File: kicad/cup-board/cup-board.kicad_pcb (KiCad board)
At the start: 4 copper layers, 68 x 68 mm, 102 parts, among them J2 EARCUP_SPKR, J7 CUP_IN (A2B + panel audio, ma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, J8 CUP_OUT (A2B to next cup), Q1 AO3401A, Q2 MMBT3904, U1 ADAU1861, U2 LSM6DSV16BX, U3 MAXM86161, U4 AQW612S, U5 AQW612S, U6 AD2428WBCPZ (sub-node), U7 TPS62161DSG (1V8), U8 ADP7118AUJZ-3.3-R7 (3V3_MIC), U9 ADP7118AUJZ-3.3-R7 (VLED)

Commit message: [LIMA] cup PCB: In1 GND / In2 1V8 planes + plane fanout; generic routing scripts in kicad/lib/route
kicad/lib/route: board-agnostic copies of the audio-board route tools (outline-based edge checks
for ring boards, env-driven plane/aircraft/fine nets, relative DSN tweaks, planes.py).
Cup: 94 pad vias + 20 EP vias, DRC 0, 153 unconnected (to route). All parts on top (Peter).

Co-Authored-By: Claude Opus 5.5 <noreply@anthropic.com>
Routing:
- net /GND: track 0.00 -> 29.2 mm, vias 0 -> 87
- net /1V8: track 0.00 -> 11.6 mm, vias 0 -> 27
- added copper zone on In2.Cu, net /1V8
- added copper zone on In1.Cu, net /GND

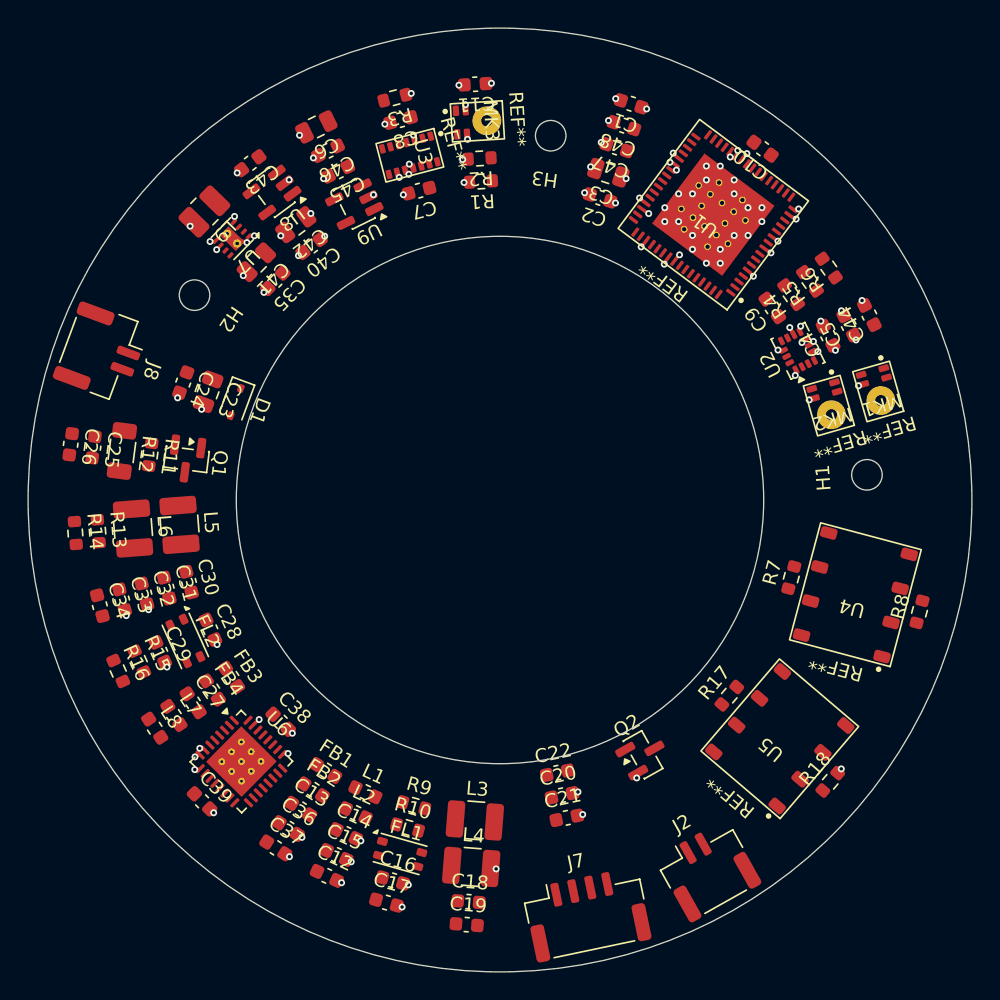
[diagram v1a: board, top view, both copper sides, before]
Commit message: [LIMA] cup PCB: Freerouting pass (WIP) - 9 unconnected; hole-clearance/neckdown fixes pending
DSN: In2 forced to plane (PLANE_LAYERS), outline inset 0.4 mm for the 0.5 mm edge rule (EDGE_INSET).

Co-Authored-By: Claude Opus 5.5 <noreply@anthropic.com>
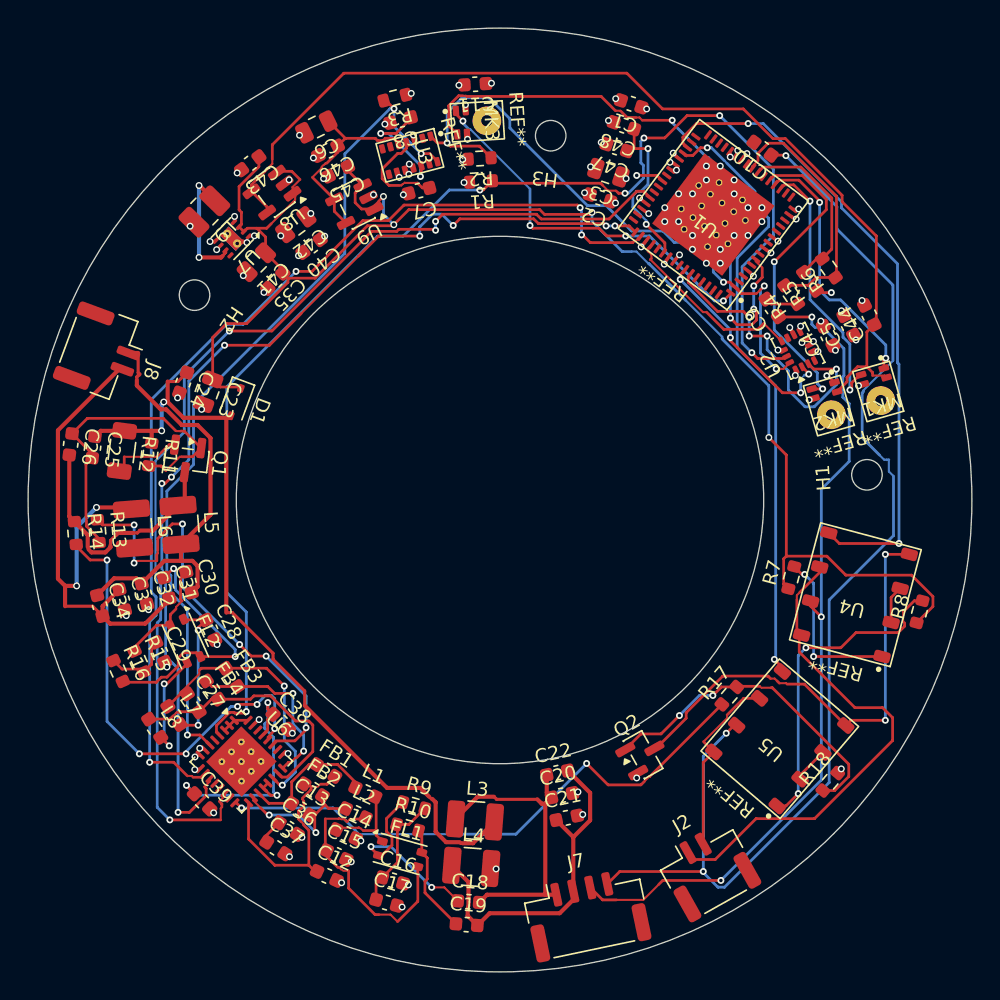
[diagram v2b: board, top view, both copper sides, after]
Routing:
- net /VIN_CUP: track 0.00 -> 112.3 mm, vias 0 -> 4
- net /SCL: track 0.00 -> 96.2 mm, vias 0 -> 6
- net /XF_SEC_B: track 0.00 -> 85.0 mm, vias 0 -> 3
- net /I2S0_SDATAO: track 0.00 -> 79.3 mm, vias 0 -> 4
- net /I2S0_FSYNC: track 0.00 -> 75.0 mm, vias 0 -> 8
- net /I2S0_BCLK: track 0.00 -> 74.5 mm, vias 0 -> 4
- net /3V3_MIC: track 0.00 -> 71.4 mm
- net /PPG_INT: track 0.00 -> 61.1 mm, vias 0 -> 3
- net /XF_SEC_A: track 0.00 -> 60.2 mm, vias 0 -> 3
- net /V_NODE: track 0.00 -> 59.5 mm, vias 0 -> 2
- net /HPOUTN: track 0.00 -> 46.8 mm, vias 0 -> 2
- net /SDA: track 0.00 -> 45.3 mm, vias 0 -> 4
- net /HPOUTP: track 0.00 -> 44.4 mm, vias 0 -> 2
- net /DMIC_CLK: track 0.00 -> 43.7 mm, vias 0 -> 4
- net /K2_CTL: track 0.00 -> 41.2 mm, vias 0 -> 2
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
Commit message: [LIMA] cup PCB: DRC-clean routing (WIP) - 8 unconnected, 0 errors; route tools: drcfix, ripnets, multi-layer maze
Co-Authored-By: Claude Opus 5.5 <noreply@anthropic.com>
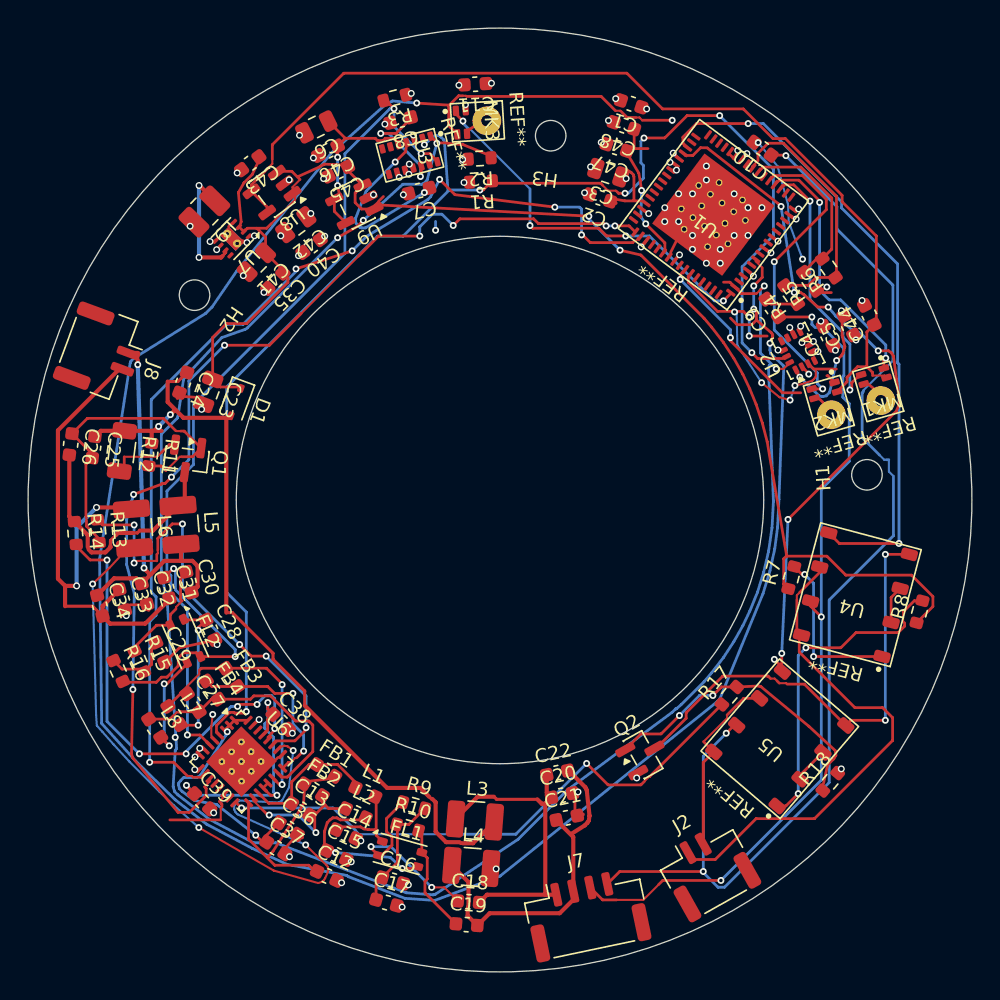
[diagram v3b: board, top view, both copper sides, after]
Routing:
- net /DMIC_CLK: track 43.7 -> 166.4 mm, vias 4 -> 5
- net /SDA: track 45.3 -> 146.2 mm, vias 4 -> 7
- net /I2S0_SDATAO: track 79.3 -> 6.61 mm, vias 4 -> 1
- net /B_VSSN: track 0.00 -> 51.0 mm, vias 0 -> 4
- net /GND: track 30.8 -> 44.9 mm, vias 87 -> 74
- net /TDM_WCLK: track 13.6 -> 0.00 mm
- net /A2B_VOUT1: track 3.76 -> 16.7 mm, vias 0 -> 2
- net Net-(C10-Pad2): track 1.12 -> 13.3 mm, vias 1 -> 3
- net /VIN_CUP: track 112.3 -> 101.5 mm, vias 4 -> 2
- net /A_ANF: track 18.3 -> 10.7 mm, vias 0 -> 2
- net /HPOUTP: track 44.4 -> 50.8 mm, vias 2 -> 7
- net /SCL: track 96.2 -> 101.8 mm, vias 6 -> 7
- net /PPG_VLDO: track 7.33 -> 12.6 mm, vias 0 -> 2
- net /1V8: track 11.6 -> 14.9 mm, vias 27 -> 24
- net /K2_B: track 23.5 -> 21.0 mm
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
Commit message: [LIMA] cup PCB: re-route around U1/U6 (WIP) - 16 unconnected, 0 errors
Co-Authored-By: Claude Opus 5.5 <noreply@anthropic.com>
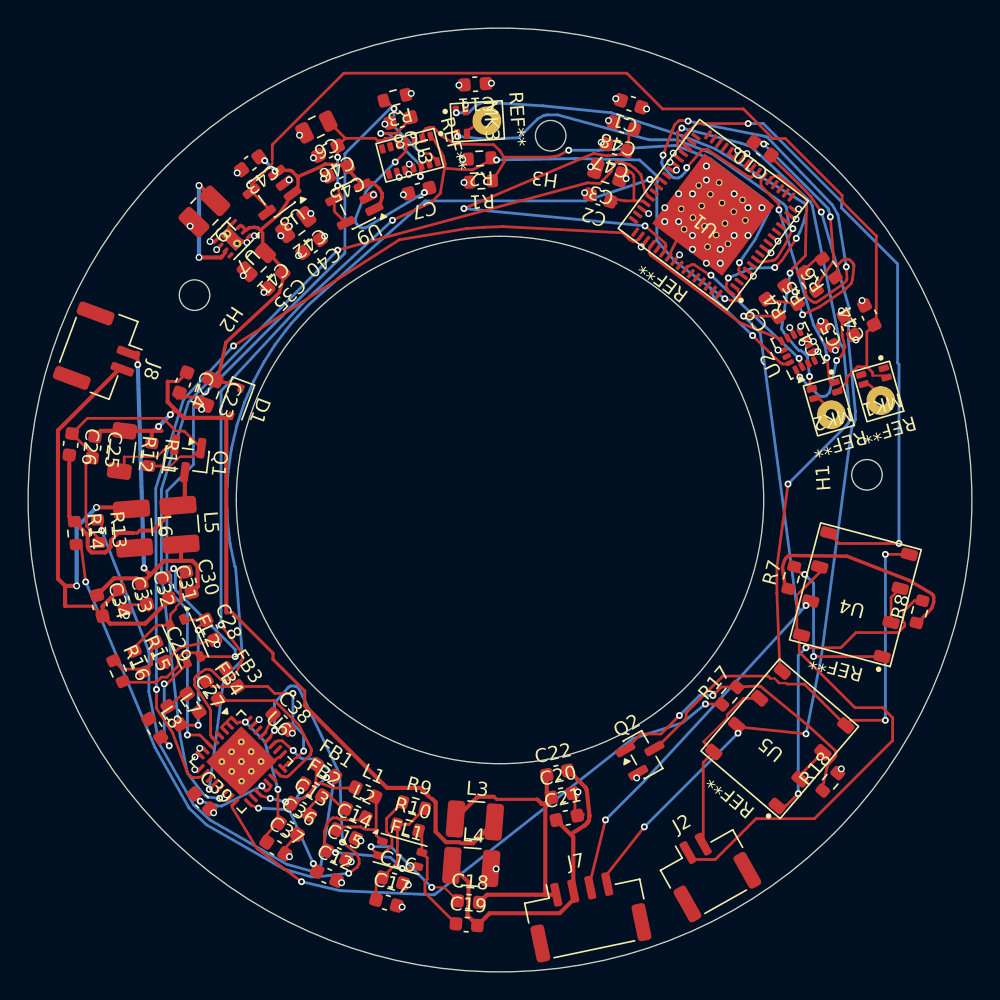
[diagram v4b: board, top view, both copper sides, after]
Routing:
- net /DMIC_CLK: track 166.4 -> 31.4 mm, vias 5 -> 2
- net /I2S0_FSYNC: track 77.2 -> 0.00 mm, vias 8 -> 0
- net /SCL: track 101.8 -> 34.4 mm, vias 7 -> 2
- net /I2S0_SDATAI: track 0.00 -> 65.7 mm, vias 0 -> 2
- net /I2S0_SDATAO: track 6.61 -> 70.9 mm, vias 1 -> 2
- net /VIN_CUP: track 101.5 -> 39.5 mm
- net /SDA: track 146.2 -> 90.3 mm, vias 7 -> 5
- net /B_VSSN: track 51.0 -> 0.00 mm, vias 4 -> 0
- net /ADC2_N: track 12.8 -> 36.6 mm, vias 0 -> 4
- net /XF_SEC_B: track 85.0 -> 61.4 mm, vias 3 -> 4
- net /TDM_BCLK: track 22.4 -> 0.00 mm, vias 6 -> 0
- net /B_SENSE: track 32.6 -> 52.8 mm, vias 6 -> 4
- net Net-(MK1-OUT-): track 19.0 -> 0.00 mm, vias 2 -> 0
- net Net-(MK1-OUT+): track 18.6 -> 0.00 mm, vias 2 -> 0
- net /B_BP: track 18.8 -> 0.74 mm, vias 2 -> 0
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
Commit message: [LIMA] cup PCB: 11 unconnected, 0 errors (WIP); maze rip-up-and-reroute + finish.sh loop
Co-Authored-By: Claude Opus 5.5 <noreply@anthropic.com>
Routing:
- net /I2S0_FSYNC: track 0.00 -> 76.3 mm, vias 0 -> 6
- net /SCL: track 34.4 -> 92.3 mm, vias 2 -> 8
- net /VIN_CUP: track 39.5 -> 84.8 mm, vias 2 -> 4
- net /B_BP: track 0.74 -> 11.5 mm, vias 0 -> 3
- net /A_AN: track 1.84 -> 7.15 mm, vias 0 -> 2

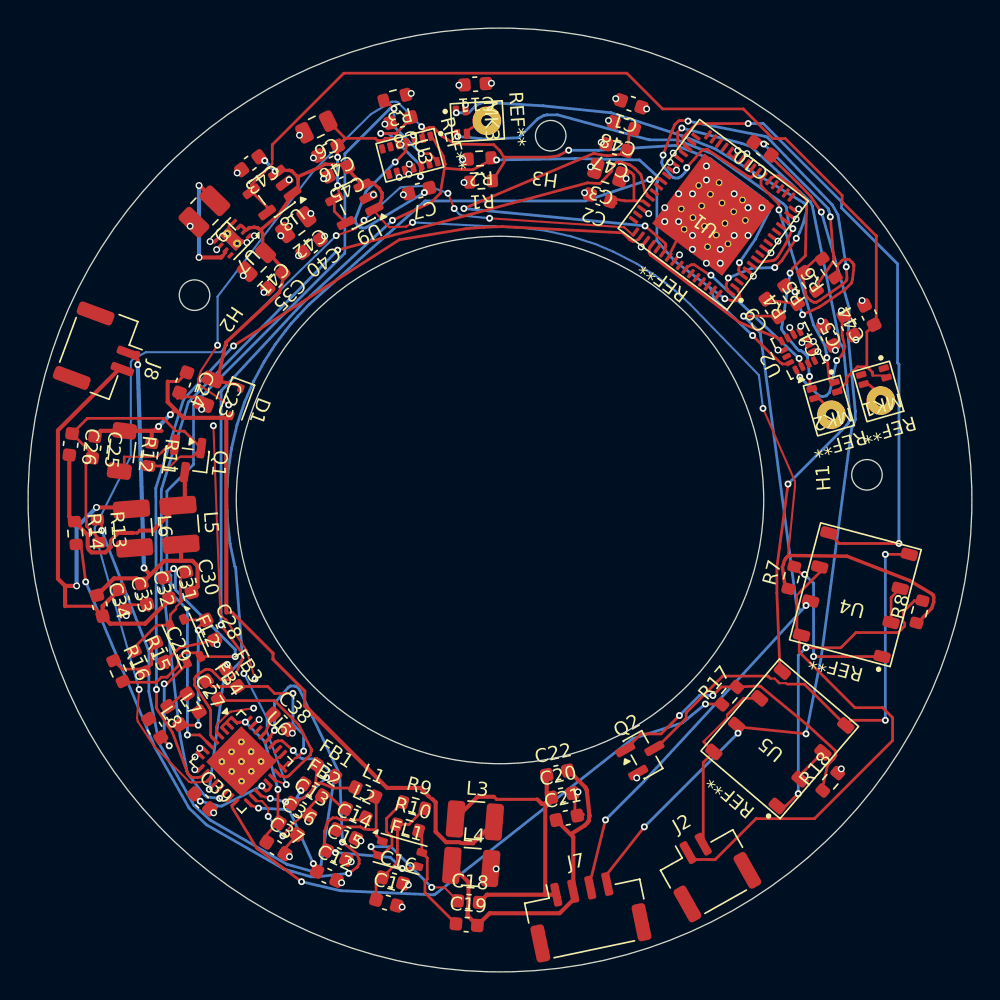
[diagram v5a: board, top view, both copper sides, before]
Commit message: [LIMA] cup PCB: U6 decaps re-placed (C35 VIN cap to pin 30, C38/C35 off U6's face); re-autorouted - 4 unconnected (WIP)
Co-Authored-By: Claude Opus 5.5 <noreply@anthropic.com>
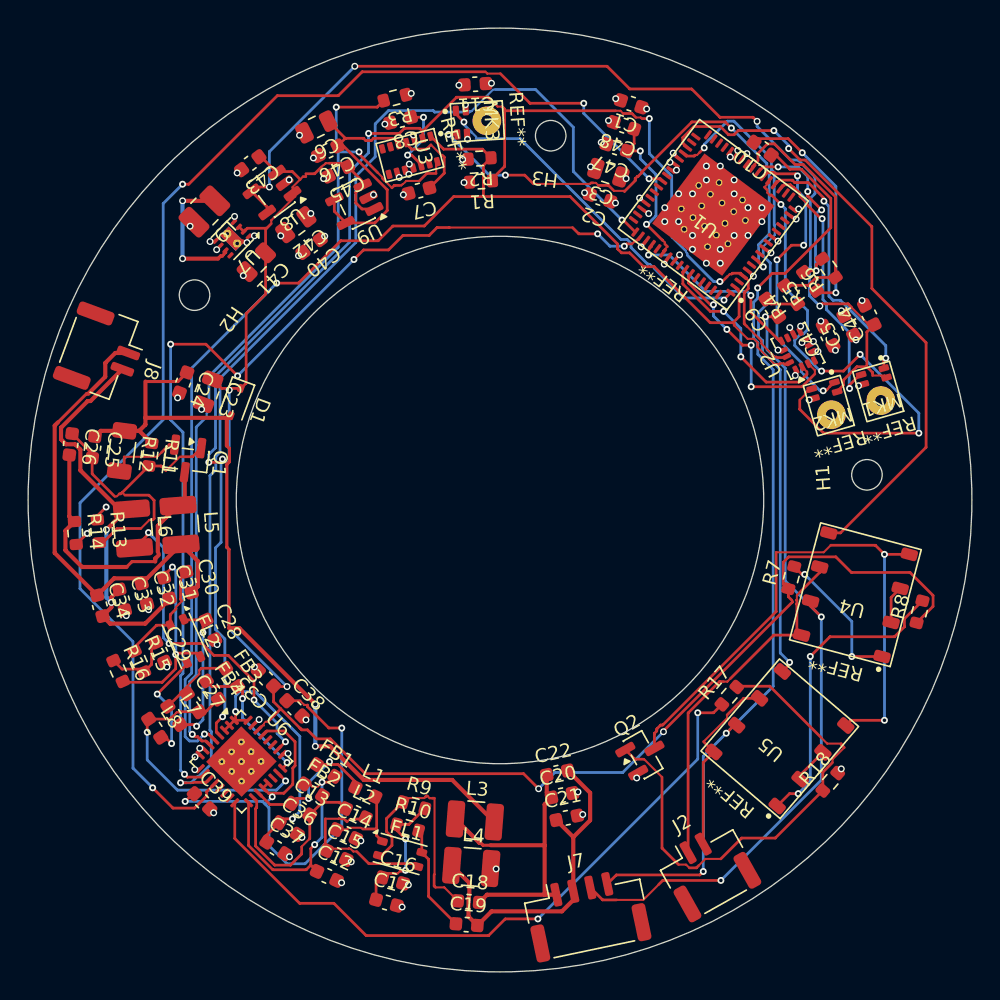
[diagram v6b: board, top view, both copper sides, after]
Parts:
- moved C35 28.7 mm to (133.1, 112.9), turned to 135 degrees
- moved C38 1.38 mm to (135.2, 115.0), turned to -45 degrees
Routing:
- net /I2S0_SDATAO: track 70.9 -> 0.00 mm, vias 2 -> 0
- net /B_SENSE: track 52.8 -> 1.12 mm, vias 4 -> 1
- net /B_SWP: track 43.9 -> 1.18 mm, vias 2 -> 1
- net /VIN_CUP: track 84.8 -> 125.2 mm
- net /A2B_VOUT2: track 6.16 -> 38.7 mm, vias 2 -> 3
- net /I2S0_SDATAI: track 65.7 -> 96.4 mm, vias 2 -> 4
- net /B_VSSN: track 0.00 -> 23.5 mm, vias 0 -> 4
- net /ADC2_N: track 36.6 -> 13.5 mm
- net Net-(MK2-OUT-): track 17.8 -> 38.5 mm, vias 2 -> 4
- net Net-(MK1-OUT-): track 0.00 -> 18.8 mm, vias 0 -> 2
- net Net-(MK1-OUT+): track 0.00 -> 18.7 mm, vias 0 -> 2
- net /U1_DVDD: track 28.2 -> 11.7 mm
- net /TDM_BCLK: track 0.00 -> 16.5 mm, vias 0 -> 4
- net /K2_B: track 21.0 -> 36.4 mm, vias 2 -> 0
- net /GND: track 44.9 -> 30.8 mm, vias 74 -> 87
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
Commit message: [LIMA] cup PCB: 7 unconnected, 0 DRC errors (WIP) - rip-up smoothing fix
Remaining 7 are U6's B-side (B_BN x3, B_SWP, B_SENSE) plus one SCL and one TDM_DATA link: U6's B-bus pins
share the A-side face, so the B pair must wrap U6 through the VIN/VOUT2 corner.
maze.py: rip-up paths are smoothed against hard+soft copper (straightened segments were cutting unripped
copper -> shorts). finish.sh never keeps a board with errors.

Co-Authored-By: Claude Opus 5.5 <noreply@anthropic.com>
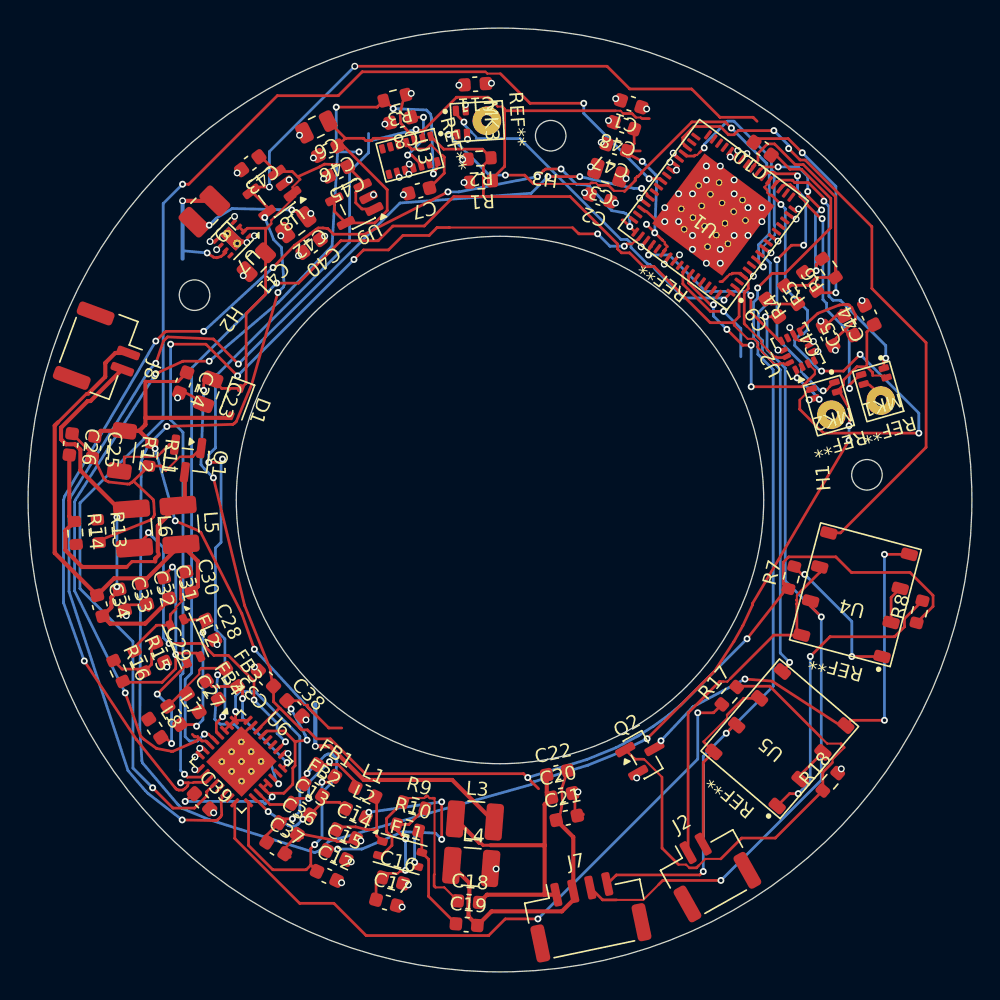
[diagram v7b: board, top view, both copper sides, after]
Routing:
- net /3V3_MIC: track 73.9 -> 169.2 mm, vias 4 -> 8
- net /I2S0_SDATAO: track 0.00 -> 84.5 mm, vias 0 -> 6
- net /B_BN: track 20.5 -> 0.00 mm, vias 2 -> 0
- net /1V8: track 11.6 -> 27.7 mm, vias 27 -> 25
- net /SCL: track 102.5 -> 88.2 mm, vias 6 -> 4
- net /A2B_VOUT2: track 38.7 -> 25.1 mm, vias 3 -> 4
- net /K2_SW: track 42.8 -> 31.9 mm, vias 2 -> 4
- net /B_BP: track 5.97 -> 16.7 mm, vias 0 -> 2
- net /PPG_INT: track 64.5 -> 75.1 mm, vias 3 -> 7
- net /GND: track 30.8 -> 40.1 mm, vias 87 -> 78
- net /TDM_DATA: track 15.1 -> 8.66 mm, vias 2 -> 1
- net /A_AN: track 14.5 -> 8.12 mm, vias 0 -> 2
- net /A_ANF: track 12.8 -> 19.1 mm, vias 0 -> 5
- net /A_ACM: track 18.0 -> 22.9 mm, vias 2 -> 3
- net /VIN_CUP: track 125.2 -> 120.7 mm
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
